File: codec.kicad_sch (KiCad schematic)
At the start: 24 parts, among them U1 UDA1380HN_N2

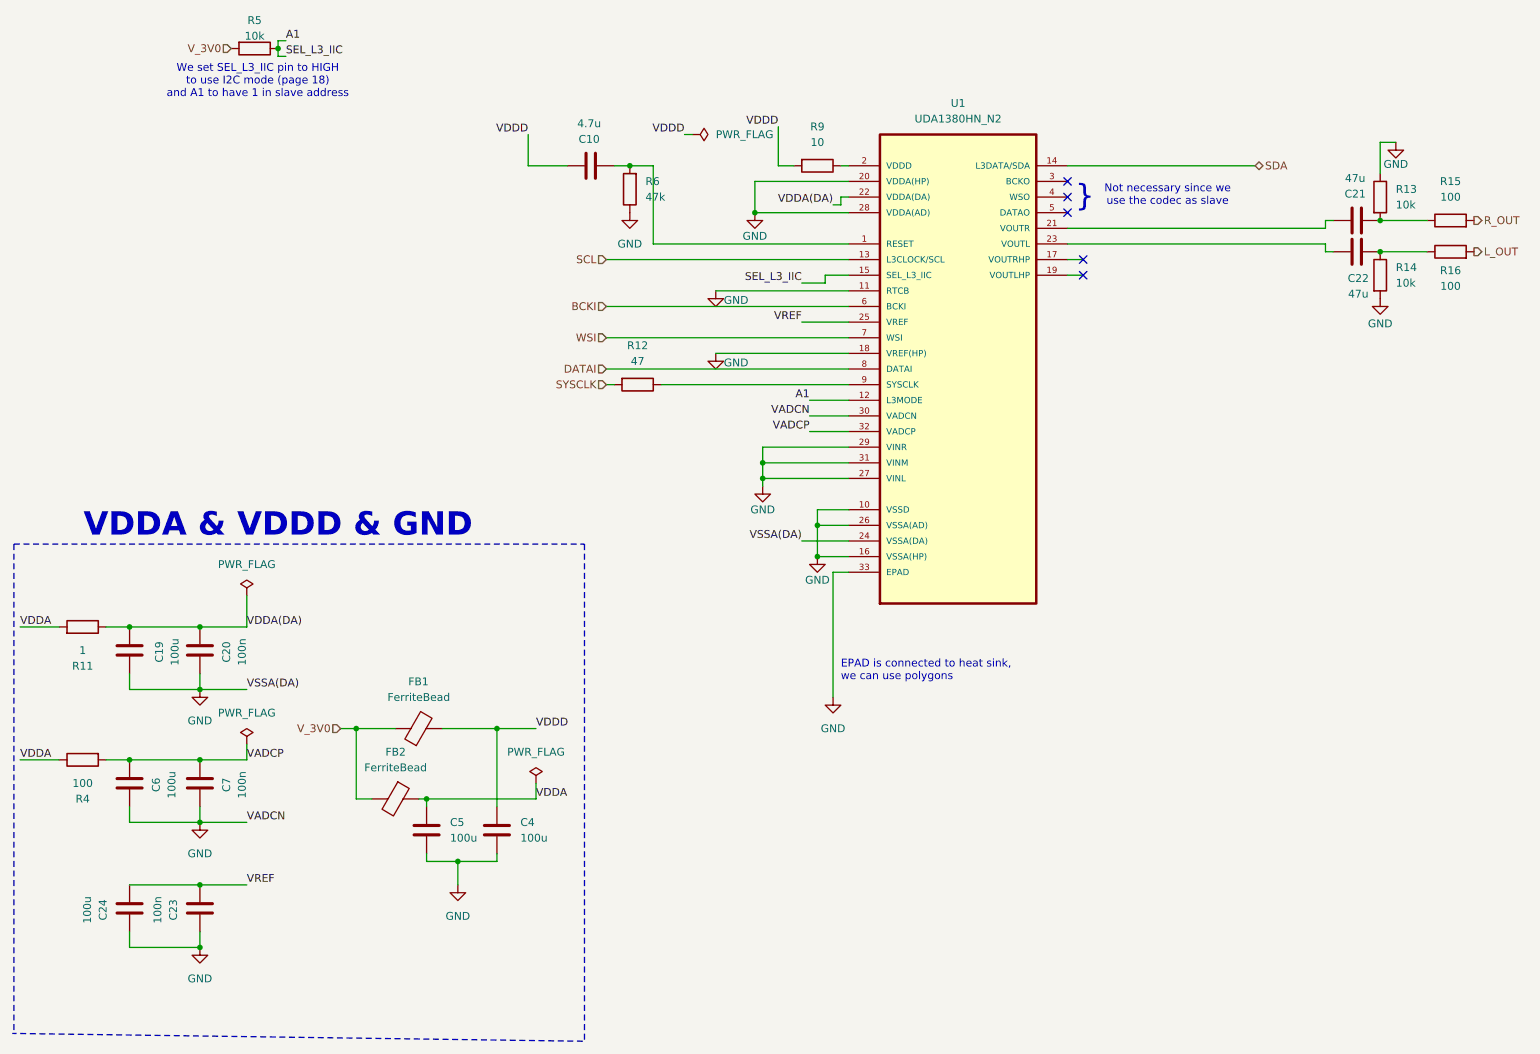
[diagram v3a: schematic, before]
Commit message: Created ESP32 footprint pads
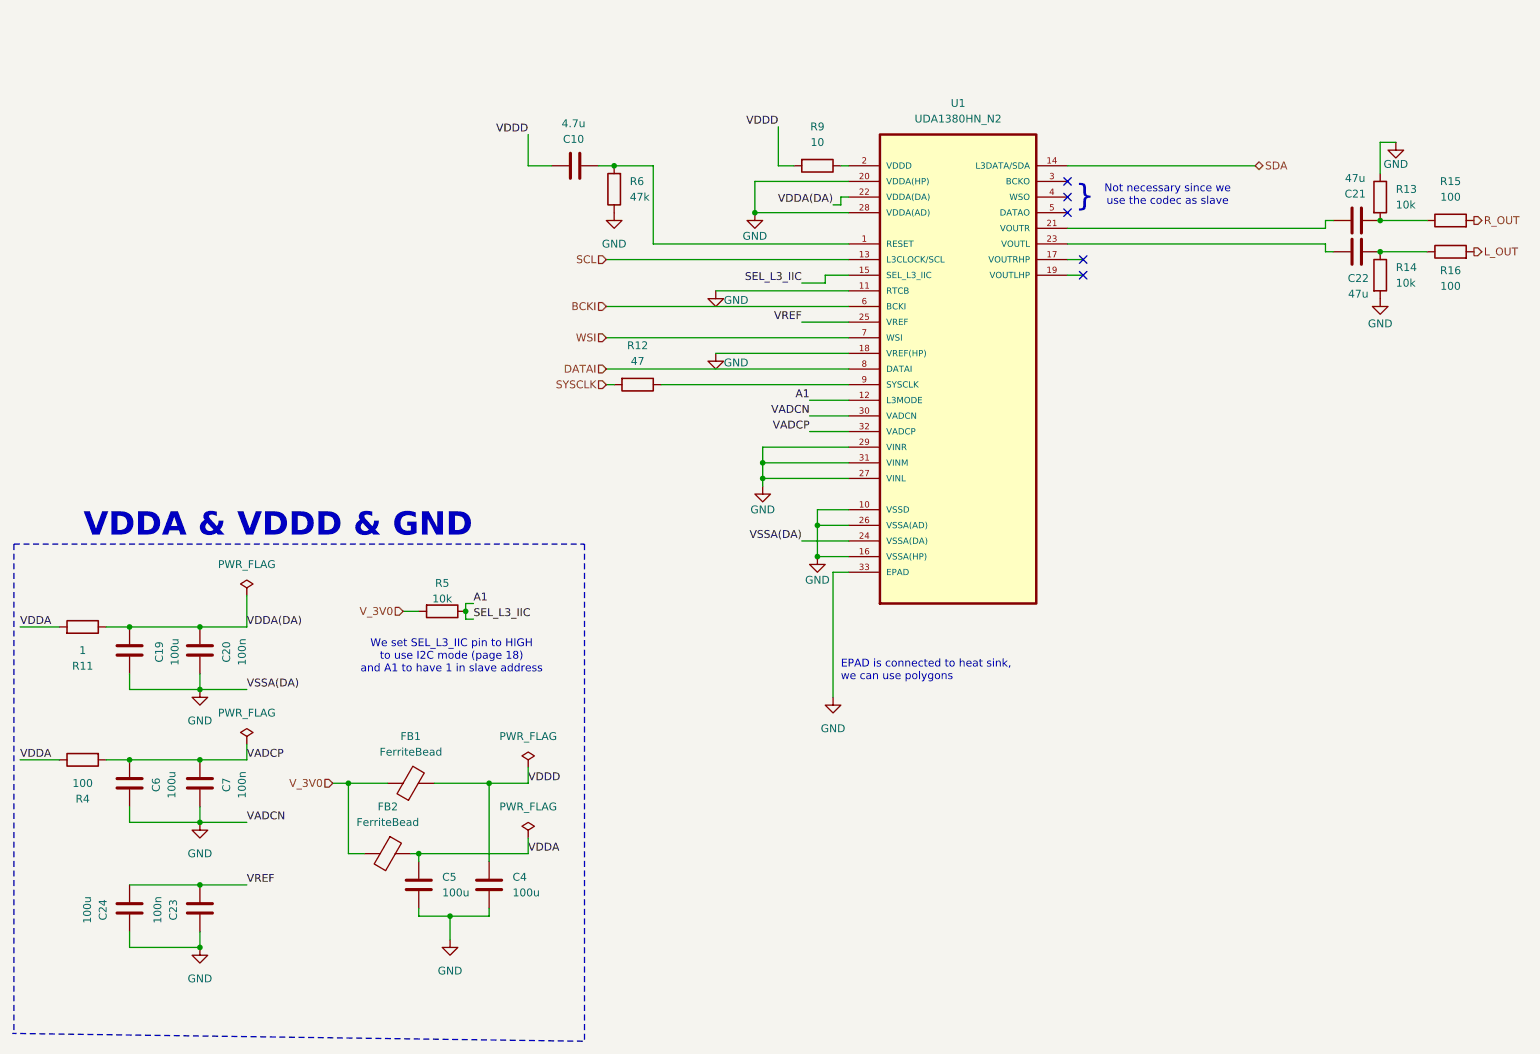
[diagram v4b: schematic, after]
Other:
- moved on the sheet: C10, C4, C5, FB1, FB2, R6

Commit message: Added basic footprint to ESP32
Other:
- title: (none) -> Audio codec
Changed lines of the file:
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@@
 	(generator_version "8.0")
 	(paper "A4")
+	(title_block
+		(title "Audio codec")
+		(date "2024-12-12")
+	)
 	(junction
 		(at 45.72 129.54)

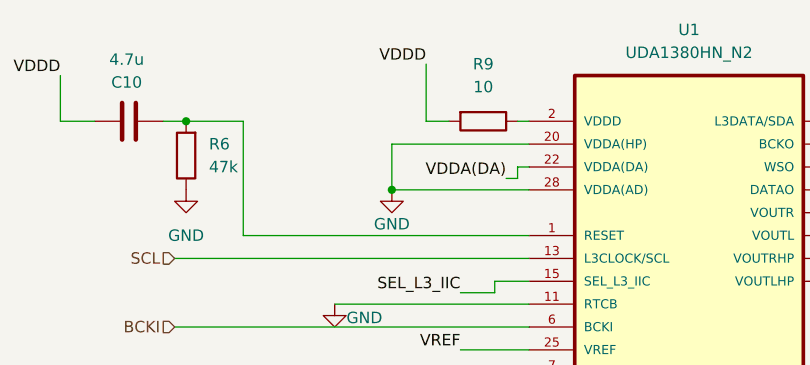
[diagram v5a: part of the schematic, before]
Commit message: Fixed STM32 footprint and added notes
SMD pads for the microcontroller and TODO list + advice from Bondyra for the design
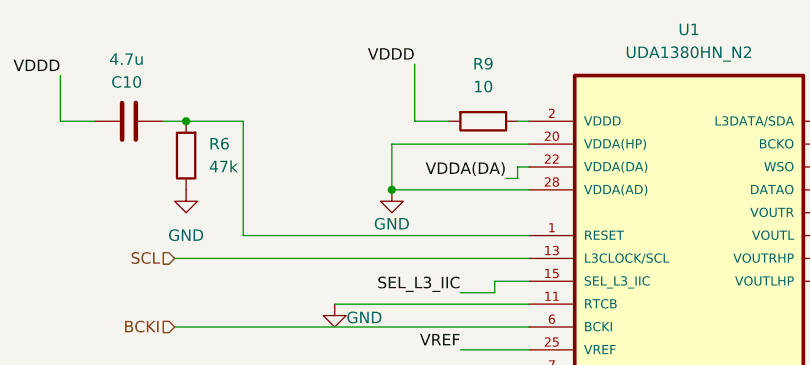
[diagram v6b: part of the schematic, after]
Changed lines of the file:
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@@
 	(wire
 		(pts
-			(xy 139.7 54.61) (xy 142.24 54.61)
+			(xy 138.43 54.61) (xy 142.24 54.61)
 		)
 		(stroke
@@
 	(wire
 		(pts
-			(xy 139.7 48.26) (xy 139.7 54.61)
+			(xy 138.43 48.26) (xy 138.43 54.61)
 		)
 		(stroke
@@
 	)
 	(label "VDDD"
-		(at 139.7 48.26 180)
-		(fields_autoplaced yes)
-		(effects
+		(at 138.43 48.26 180)
+		(fields_autoplaced yes)
+		(effects

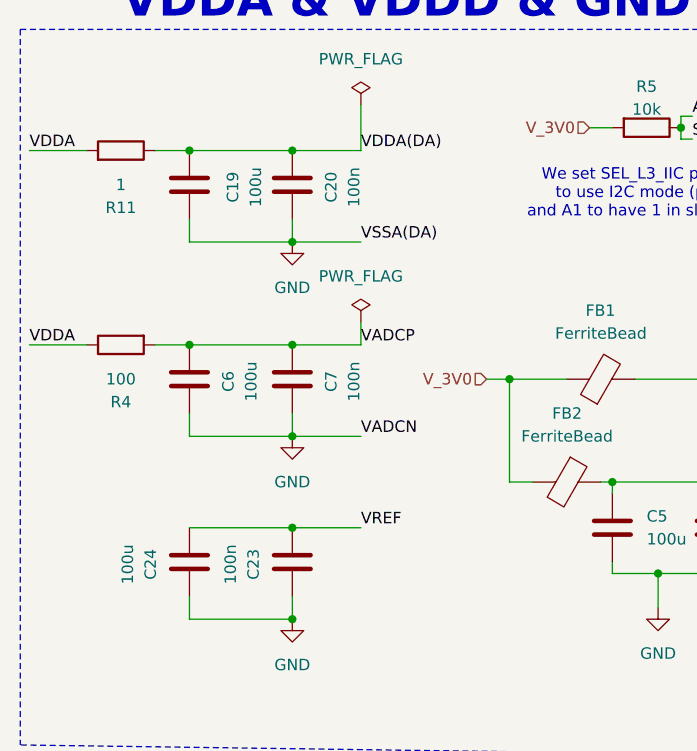
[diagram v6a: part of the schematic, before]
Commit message: Added footprints and imported to PCB
All of them except speakers
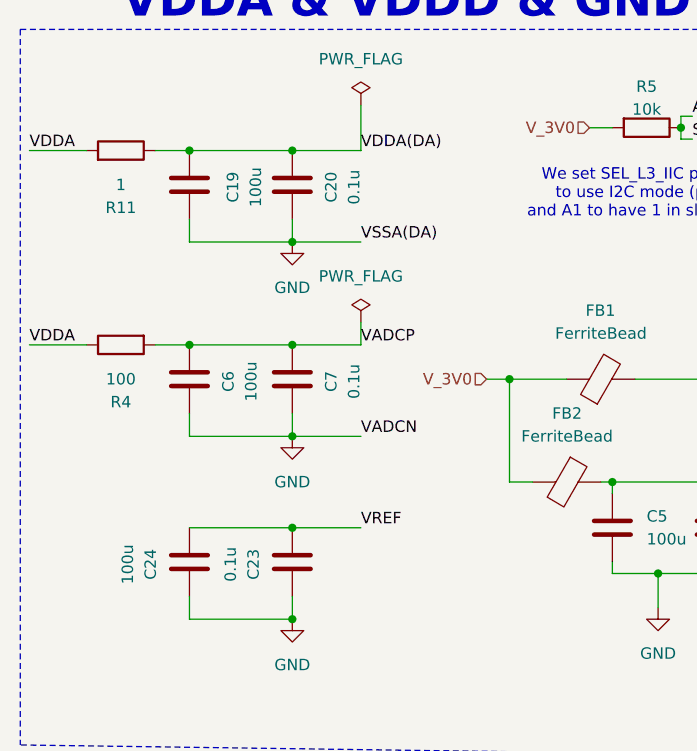
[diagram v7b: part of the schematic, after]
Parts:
- C10, C19, C21, C22, C24, C4, C5, C6: footprint (none) -> Capacitor_SMD:C_0603_1608Metric
- C20, C23, C7: value 100n -> 0.1u; footprint (none) -> Capacitor_SMD:C_0603_1608Metric
- FB1, FB2: footprint (none) -> OtherComponents:FerriteBead_742861160_0603
- R11, R12, R13, R14, R15, R16, R4, R5, R6, R9: footprint (none) -> Resistor_SMD:R_0603_1608Metric
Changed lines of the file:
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@@
 			)
 		)
-		(property "Footprint" ""
+		(property "Footprint" "OtherComponents:FerriteBead_742861160_0603"
 			(at 80.01 156.718 90)
 			(effects
@@
 			)
 		)
-		(property "Footprint" ""
+		(property "Footprint" "Resistor_SMD:R_0603_1608Metric"
 			(at 146.05 52.832 90)
 			(effects
@@
 			)
 		)
-		(property "Value" "100n"
+		(property "Value" "0.1u"
 			(at 52.578 155.194 90)
 			(effects
@@
 			)
 		)
-		(property "Footprint" ""
+		(property "Footprint" "Capacitor_SMD:C_0603_1608Metric"
 			(at 46.6852 151.13 0)
 			(effects
@@
 			)
 		)
-		(property "Footprint" ""
+		(property "Footprint" "Resistor_SMD:R_0603_1608Metric"
 			(at 85.09 125.222 90)
 			(effects
@@
 			)
 		)
-		(property "Footprint" ""
+		(property "Footprint" "Resistor_SMD:R_0603_1608Metric"
 			(at 26.67 149.352 90)
 			(effects
@@
 			)
 		)
-		(property "Value" "100n"
+		(property "Value" "0.1u"
 			(at 52.578 133.604 90)
 			(effects
@@
 			)
 		)
-		(property "Footprint" ""
+		(property "Footprint" "Capacitor_SMD:C_0603_1608Metric"
 			(at 46.6852 129.54 0)
 			(effects
@@
 			)
 		)
-		(property "Footprint" ""
+		(property "Footprint" "Resistor_SMD:R_0603_1608Metric"
 			(at 248.92 65.278 90)
 			(effects
@@
 			)
 		)
-		(property "Footprint" ""
+		(property "Footprint" "Capacitor_SMD:C_0603_1608Metric"
 			(at 93.6752 175.26 0)
 			(effects
@@
 			)
 		)
-		(property "Footprint" ""
+		(property "Footprint" "Capacitor_SMD:C_0603_1608Metric"
 			(at 33.3248 171.45 0)
 			(effects
@@
 			)
 		)
-		(property "Footprint" ""
+		(property "Footprint" "Capacitor_SMD:C_0603_1608Metric"
 			(at 35.2552 151.13 0)
 			(effects
@@
 			)
 		)
-		(property "Footprint" ""
+		(property "Footprint" "OtherComponents:FerriteBead_742861160_0603"
 			(at 76.2 164.592 90)
 			(effects
@@
 			)
 		)
-		(property "Footprint" ""
+		(property "Footprint" "Resistor_SMD:R_0603_1608Metric"
 			(at 116.84 88.392 90)
 			(effects
@@
 			)
 		)
-		(property "Footprint" ""
+		(property "Footprint" "Capacitor_SMD:C_0603_1608Metric"
 			(at 237.49 62.5348 0)
 			(effects
@@
 			)
 		)
-		(property "Footprint" ""
+		(property "Footprint" "Capacitor_SMD:C_0603_1608Metric"
 			(at 229.87 69.5452 0)
 			(effects
@@
 			)
 		)
-		(property "Footprint" ""
+		(property "Footprint" "Resistor_SMD:R_0603_1608Metric"
 			(at 26.67 131.318 90)
 			(effects
@@
 			)
 		)
-		(property "Value" "100n"
+		(property "Value" "0.1u"
 			(at 38.862 175.514 90)
 			(effects
@@
 			)
 		)
-		(property "Footprint" ""
+		(property "Footprint" "Capacitor_SMD:C_0603_1608Metric"
 			(at 44.7548 171.45 0)
 			(effects
@@
 			)
 		)
-		(property "Footprint" ""
+		(property "Footprint" "Capacitor_SMD:C_0603_1608Metric"
 			(at 110.49 53.6448 0)
 			(effects
@@
 			)
 		)
-		(property "Footprint" ""
+		(property "Footprint" "Capacitor_SMD:C_0603_1608Metric"
 			(at 82.2452 175.26 0)
 			(effects
@@
 			)
 		)
-		(property "Footprint" ""
+		(property "Footprint" "Resistor_SMD:R_0603_1608Metric"
 			(at 235.712 72.39 90)
 			(effects
@@
 			)
 		)
-		(property "Footprint" ""
+		(property "Footprint" "Resistor_SMD:R_0603_1608Metric"
 			(at 114.808 58.42 90)
 			(effects
@@
 			)
 		)
-		(property "Footprint" ""
+		(property "Footprint" "Capacitor_SMD:C_0603_1608Metric"
 			(at 35.2552 129.54 0)
 			(effects
@@
 			)
 		)
-		(property "Footprint" ""
+		(property "Footprint" "Resistor_SMD:R_0603_1608Metric"
 			(at 248.92 70.358 90)
 			(effects
@@
 			)
 		)
-		(property "Footprint" ""
+		(property "Footprint" "Resistor_SMD:R_0603_1608Metric"
 			(at 235.712 59.69 90)
 			(effects
